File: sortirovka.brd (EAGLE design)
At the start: 40 parts, among them IC1 DS1307/PCF8583, U1 MAX3485CSA, X1 PI3-CONMINIBOARD, X10 MKDSN1,5/3-5,08, X3 MKDSN1,5/4-5,08, X4 MKDSN1,5/2-5,08, X6 22-23-2051

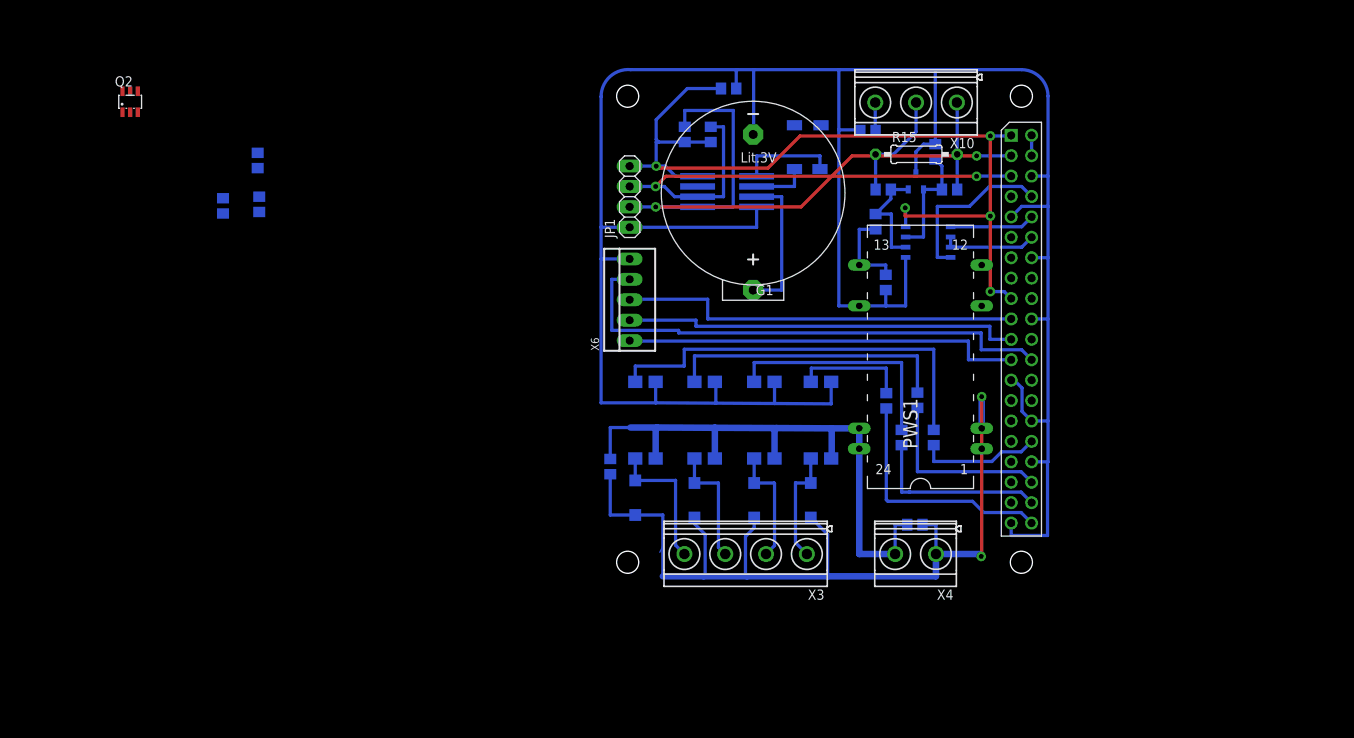
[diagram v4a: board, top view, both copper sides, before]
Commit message: could be produced
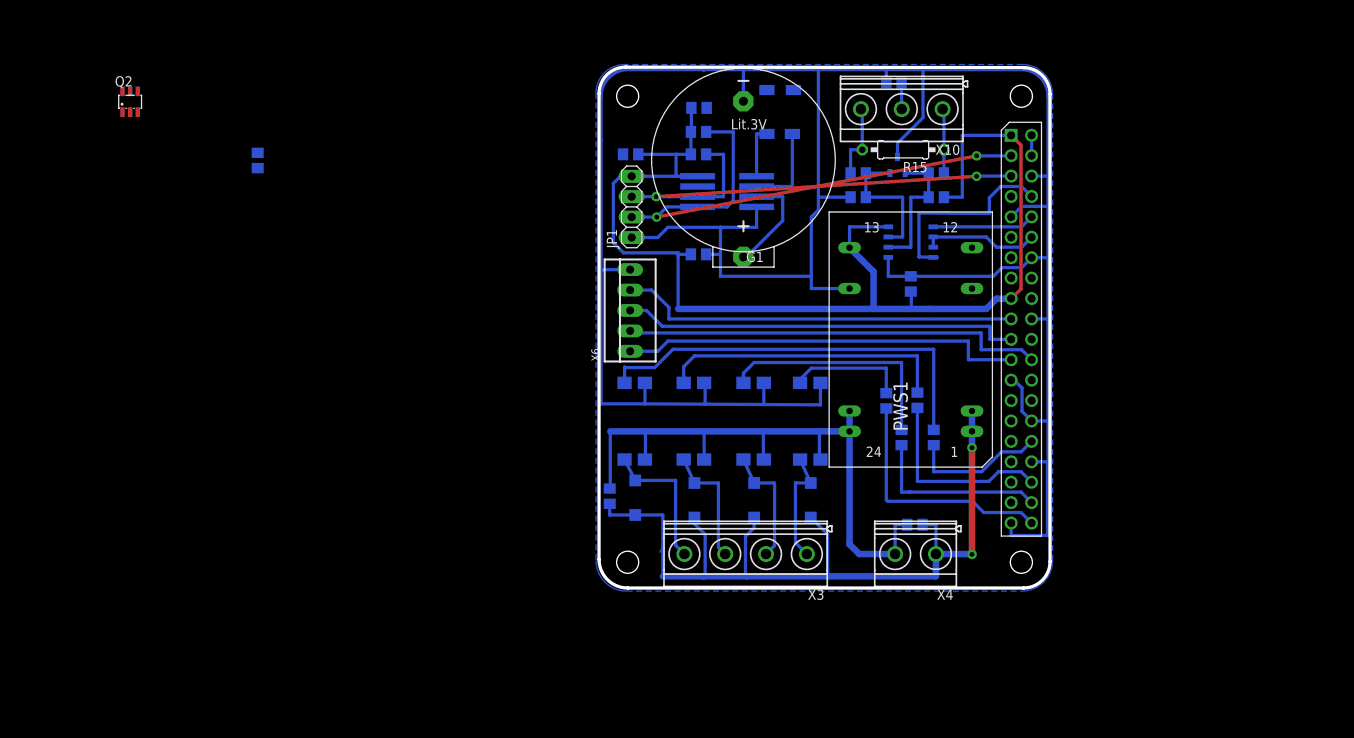
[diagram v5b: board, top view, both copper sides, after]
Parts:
- PWS1: value TEN_32410 -> TEN_32410-1; device traco-electronic:TEN3XXXX -> MyLib:TEN3-XXXX
- moved C9 60.5 mm to (5.78, 70.5), turned to 180 degrees
- moved C5 55.0 mm to (5.71, 52.3), turned to 180 degrees
- moved C8 14.7 mm to (-2.73, 64.7), turned to 0 degrees
- moved R7 11.5 mm to (25.6, 62.4), turned to 0 degrees
- moved R5 11.1 mm to (25.6, 59.4), turned to 0 degrees
- moved R6 8.15 mm to (35.3, 59.4), turned to 0 degrees
- moved R8 6.91 mm to (35.3, 62.4), turned to 180 degrees
- moved R9 6.85 mm to (30.0, 73.7)
- moved Q1 5.56 mm to (15.5, 69.8)
- moved G1 4.30 mm to (11.3, 64.0)
- moved C6 3.68 mm to (-5.33, 22.2)
- moved C10 3.12 mm to (32.1, 48.6), turned to 90 degrees
- moved U$3 3.06 mm to (30.5, 63.4)
- moved R10 2.91 mm to (5.71, 64.7), turned to 0 degrees
- moved PWS1 2.47 mm to (32.1, 41.7)
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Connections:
- removed net N$47: R6.2, R8.1, U$3.2, U1.6
- removed net N$9: IC1.2, Q1.1
- new net A+: R6.2, R8.1, U$3.1, U1.6
- new net B-: R5.1, R7.1, U$3.2, U1.7
- net MISO: now also X6.3; no longer X6.2
- net MOSI: now also X6.4; no longer X6.3
- net N$4: now also IC1.1, Q1.1; no longer R5.1, R7.1, U$3.1, U1.7
- net N$45: now also X10.3; no longer X10.1
- net N$46: now also X10.1; no longer X10.2
- net N$5: now also X10.2; no longer X10.3
- net N$8: now also IC1.2; no longer IC1.1
- net SPI0: now also X6.2; no longer X6.4
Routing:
- net +3V3: track 125.0 -> 148.8 mm, vias 5 -> 0
- net B-: track 0.00 -> 17.3 mm
- net A+: track 0.00 -> 17.2 mm
- net GND: track 317.7 -> 334.3 mm
- net N$47: track 13.9 -> 0.00 mm
- net GND1: track 115.1 -> 104.0 mm
- net SPI0: track 63.7 -> 52.8 mm
- net SDA: track 79.9 -> 70.3 mm
- net N$4: track 14.5 -> 6.55 mm
- net N$9: track 6.87 -> 0.00 mm
- net N$46: track 14.2 -> 8.15 mm
- net N$3: track 18.3 -> 13.0 mm
- net SCL: track 67.3 -> 63.1 mm
- net TX: track 21.3 -> 24.8 mm
- net +24V: track 75.6 -> 79.1 mm
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- added copper zone on layer 16, net GND
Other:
- board outline added: 56.1 x 64.8 mm

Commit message: not diode - supreesor
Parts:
- removed C6, C7: 0.1, rcl:C0805
- removed Q2: (no value), MyLib:SOT23-6
- D1, D2, D3, D4: value DIODE1N4007 -> BAV199; device MyLib:SMA-DIODE -> MyLib:SOT23
- moved D1 15.0 mm to (-2.29, 22.7), turned to 0 degrees
- moved D3 14.8 mm to (12.6, 22.7), turned to 0 degrees
- moved R4 8.94 mm to (27.7, 25.2)
- moved R1 8.80 mm to (37.0, 38.0)
- moved D4 1.08 mm to (19.6, 22.7), turned to 0 degrees
- moved R2 0.90 mm to (33.8, 34.0)
- moved D2 0.76 mm to (5.21, 22.4), turned to 0 degrees
- moved R3 0.19 mm to (30.8, 29.5)
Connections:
- removed net N$13 (its old number): D3.C, OC7.4, X3.4
- removed net N$14: Q2.1, Q2.2, Q2.5, Q2.6
- new net N$9: D1.3, OC7.4, X3.4
- net +24V: now also D1.2, D2.2, D3.2, D4.2; no longer C6.1
- net +3V3: no longer C7.1
- net GND: no longer C7.2
- net GND1: now also D1.1, D2.1, D3.1, D4.1; no longer C6.2, D1.A, D2.A, D3.A, D4.A, Q2.3
- net N$10: now also D4.3; no longer D4.C
- net N$11: now also D3.3; no longer D1.C
- net N$12: now also D2.3; no longer D2.C
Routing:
- net +24V: track 79.1 -> 111.9 mm
- net N$13 (its old number): track 17.6 -> 0.00 mm
- net N$9: track 0.00 -> 16.3 mm
- net GND: track 334.3 -> 319.5 mm
- net N$24: track 0.00 -> 13.3 mm
- net N$16: track 0.00 -> 9.52 mm
- net N$29: track 14.9 -> 22.7 mm
- net N$2: track 30.7 -> 23.3 mm
- net N$6: track 17.0 -> 23.7 mm
- net N$15: track 51.5 -> 44.9 mm
- net N$25: track 0.00 -> 5.33 mm
- net N$21: track 0.00 -> 4.64 mm
- net GND1: track 104.0 -> 106.4 mm
- net +3V3: track 148.8 -> 146.7 mm
- net N$10: track 14.6 -> 15.7 mm
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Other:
- board text added: "nte.spb.ru srt1-2.1"

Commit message: wip
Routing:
- net GND: track 319.5 -> 324.2 mm
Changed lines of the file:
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@@
 <wire x1="49.149" y1="26.4414" x2="47.1678" y2="26.4414" width="0.4064" layer="16"/>
 <wire x1="49.2125" y1="26.4414" x2="49.2125" y2="31.5214" width="0.4064" layer="16"/>
-<wire x1="-6.4135" y1="66.3575" x2="-6.4135" y2="50.3555" width="0.4064" layer="16"/>
+<wire x1="-6.4135" y1="64.8335" x2="-6.4135" y2="66.3575" width="0.4064" layer="16"/>
+<wire x1="-6.4135" y1="64.8335" x2="-6.4135" y2="50.3555" width="0.4064" layer="16"/>
 <wire x1="-6.4135" y1="66.3575" x2="-6.4135" y2="71.882" width="0.4064" layer="16"/>
 <wire x1="-6.4135" y1="71.882" x2="-2.7305" y2="75.2475" width="0.4064" layer="16" curve="-95.158311"/>
-<wire x1="6.4135" y1="75.2475" x2="11.2395" y2="75.2475" width="0.4064" layer="16"/>
+<wire x1="6.7945" y1="75.2475" x2="6.4135" y2="75.2475" width="0.4064" layer="16"/>
+<wire x1="6.7945" y1="75.2475" x2="11.2395" y2="75.2475" width="0.4064" layer="16"/>
 <wire x1="6.4135" y1="75.2475" x2="-2.7305" y2="75.2475" width="0.4064" layer="16"/>
 <wire x1="44.6278" y1="18.8214" x2="44.6278" y2="17.272" width="0.4064" layer="16"/>
@@
 <wire x1="8.5725" y1="55.499" x2="8.4455" y2="55.626" width="0.4064" layer="16"/>
 <contactref element="PWS1" pad="16"/>
-<wire x1="20.66925" y1="57.81675" x2="19.7485" y2="56.896" width="0.4064" layer="16"/>
 <wire x1="-0.9525" y1="33.655" x2="-6.4135" y2="33.655" width="0.4064" layer="16"/>
 <wire x1="-6.4135" y1="33.655" x2="-6.4135" y2="50.3555" width="0.4064" layer="16"/>
 <wire x1="8.4455" y1="52.1335" x2="8.4455" y2="55.626" width="0.4064" layer="16"/>
 <wire x1="20.6375" y1="59.4995" x2="20.6375" y2="75.2475" width="0.4064" layer="16"/>
-<wire x1="20.6375" y1="59.4995" x2="20.6375" y2="57.8485" width="0.4064" layer="16"/>
-<wire x1="20.6375" y1="57.8485" x2="20.66925" y2="57.81675" width="0.4064" layer="16"/>
 <wire x1="33.655" y1="75.2475" x2="33.655" y2="69.2785" width="0.4064" layer="16"/>
 <wire x1="33.655" y1="69.2785" x2="30.48" y2="66.1035" width="0.4064" layer="16"/>
@@
 <wire x1="48.3743" y1="32.7152" x2="48.387" y2="32.7025" width="0.3048" layer="16" curve="-90"/>
 <wire x1="48.387" y1="32.7025" x2="49.2125" y2="32.7025" width="0.3048" layer="16"/>
+<wire x1="6.7285" y1="70.485" x2="6.7945" y2="70.485" width="0.4064" layer="16"/>
+<wire x1="6.7945" y1="70.485" x2="6.7945" y2="75.2475" width="0.4064" layer="16"/>
+<wire x1="-3.6805" y1="64.7065" x2="-6.4135" y2="64.7065" width="0.4064" layer="16"/>
+<wire x1="-6.4135" y1="64.7065" x2="-6.4135" y2="64.8335" width="0.4064" layer="16"/>
+<wire x1="45.974" y1="35.6235" x2="45.974" y2="35.2425" width="0" layer="19" extent="16-16"/>
+<wire x1="-2.6035" y1="54.356" x2="-2.794" y2="50.3555" width="0" layer="19" extent="1-1"/>
+<wire x1="24.511" y1="48.006" x2="29.331" y2="49.5275" width="0" layer="19" extent="16-16"/>
 </signal>
 <signal name="N$6">

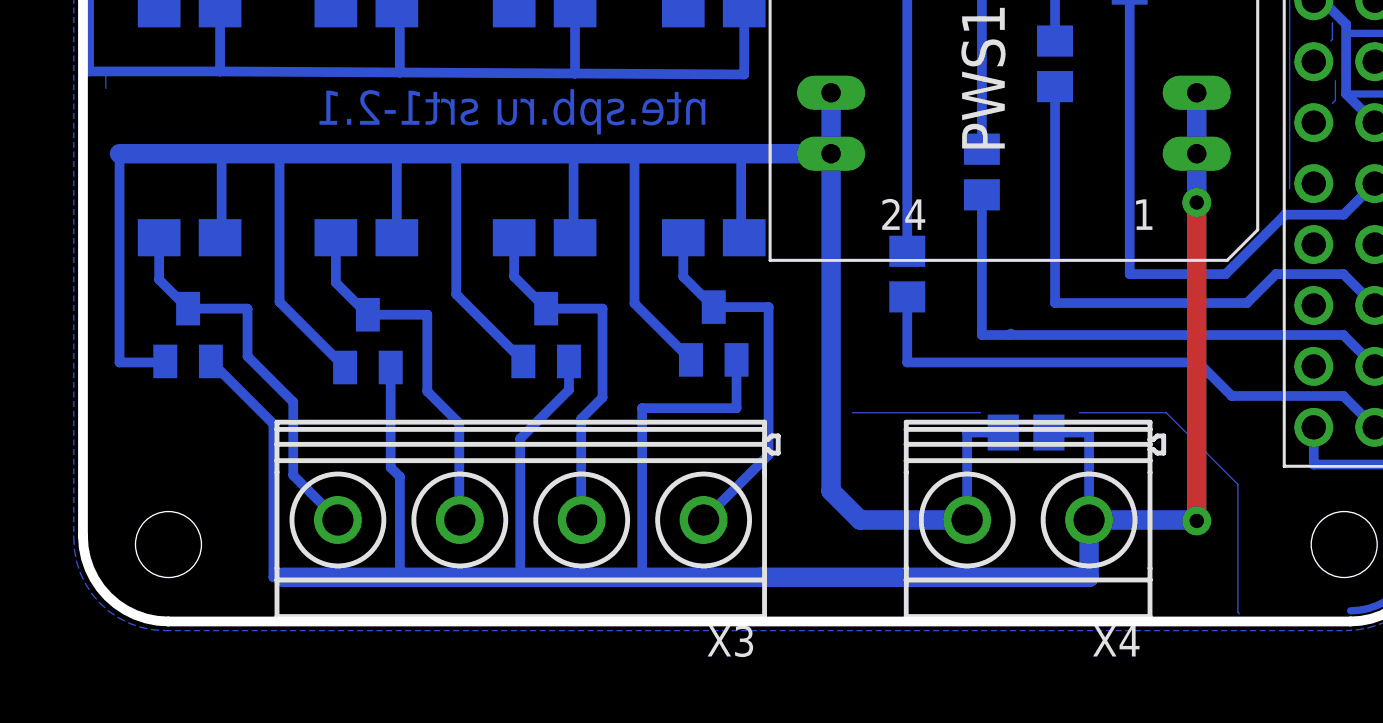
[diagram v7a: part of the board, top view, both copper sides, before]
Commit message: current source for optocoupler, old design
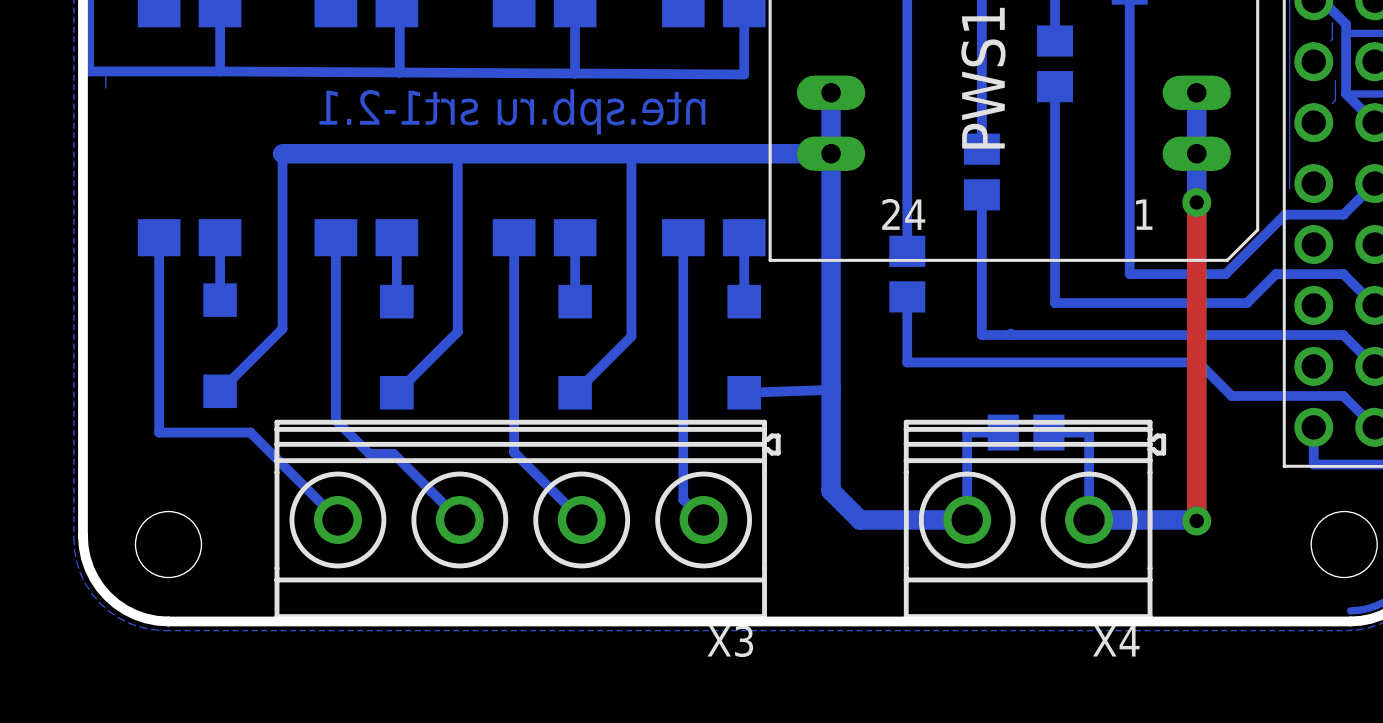
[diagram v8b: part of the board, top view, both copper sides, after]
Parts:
- removed D1, D2, D3, D4: BAV199, MyLib:SOT23
- added U$1, U$2, U$4, U$5: NSI45020AT1GSOD-123, MyLib:SOD123
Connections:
- new net N$14: OC10.3, U$5.C
- new net N$17: OC9.3, U$1.C
- new net N$20: OC8.3, U$4.C
- new net N$30: OC7.3, U$2.C
- net +24V: now also U$1.A, U$2.A, U$4.A, U$5.A; no longer D1.2, D2.2, D3.2, D4.2, OC10.3, OC7.3, OC8.3, OC9.3
- net GND1: no longer D1.1, D2.1, D3.1, D4.1
- net N$10: no longer D4.3
- net N$11: no longer D3.3
- net N$12: no longer D2.3
- net N$9: no longer D1.3
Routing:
- net GND1: track 106.4 -> 27.7 mm
- net +24V: track 111.9 -> 87.3 mm
- net N$24: track 13.3 -> 0.00 mm
- net N$25: track 5.33 -> 0.00 mm
- net N$10: track 15.7 -> 12.1 mm
- net N$20: track 0.00 -> 2.66 mm
- net N$17: track 0.00 -> 2.66 mm
- net N$14: track 0.00 -> 2.66 mm
- net N$30: track 0.00 -> 2.60 mm
- net N$11: track 15.0 -> 12.9 mm
- net N$12: track 15.4 -> 14.5 mm
- net N$9: track 16.3 -> 17.1 mm
